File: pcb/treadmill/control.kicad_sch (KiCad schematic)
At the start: 42 parts, among them J6 TO-DISPLAY, J7 JK1 (PROG), J8 MOTOR, Q3 "2T1" SS9012 PNP, Q4 "J3" SS9013 NPN, U4 STM8S003F3P, U5 EL817, U6 EL817, U7 LM358_DFN, U8 LM358_DFN

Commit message: Sustained progress reversing the pcb
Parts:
- added C13: C, symbol Device:C
- added C?: C_Polarized, symbol Device:C_Polarized
- added D3: LED, symbol Device:LED
- added Q11: "2T1" SS9012 PNP, symbol Simulation_SPICE:PNP
- added R14: 2k, symbol Device:R
- added R49: OL, symbol Device:R
- added U5: HL05, symbol Regulator_Linear:AZ1117-5.0
- added U8: EL817, Package_DIP:DIP-4_W7.62mm, symbol Isolator:EL817
- R50: value inf -> OL
- renumbered U5 to U6, U6 to U7
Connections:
- net +5V: now also D3.2 (A)
- net GND: now also C13.2, U5.1 (GND), U8.2
- net at R12.2, U6.1: now also C13.1, U5.2 (VO)
- net at C10.1: now also U5.3 (VI), U8.3
- net at R50.2: now also U8.4
- new net: R49.1, U8.1
- new net: D3.1 (K), R14.2
- new net: C?.2, R49.2
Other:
- moved on the sheet: BR1, C10, C14, C15, C17, C18, C19, C20, C23, C27, C3, C31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

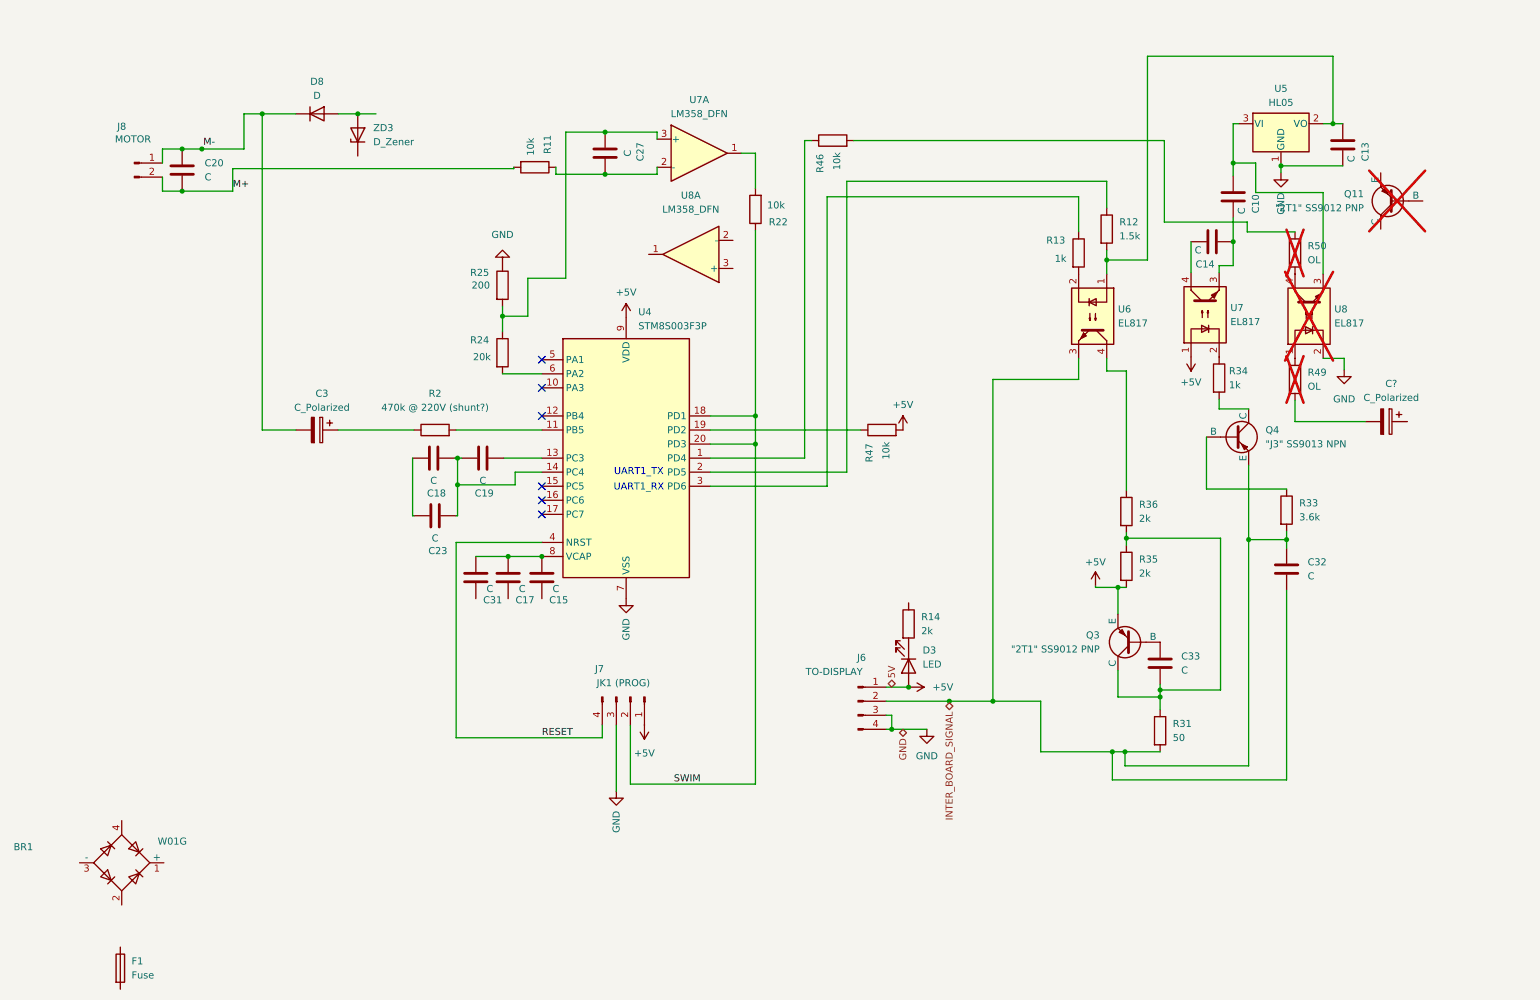
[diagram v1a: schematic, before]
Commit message: Figuring out more connections from the control board, mostly
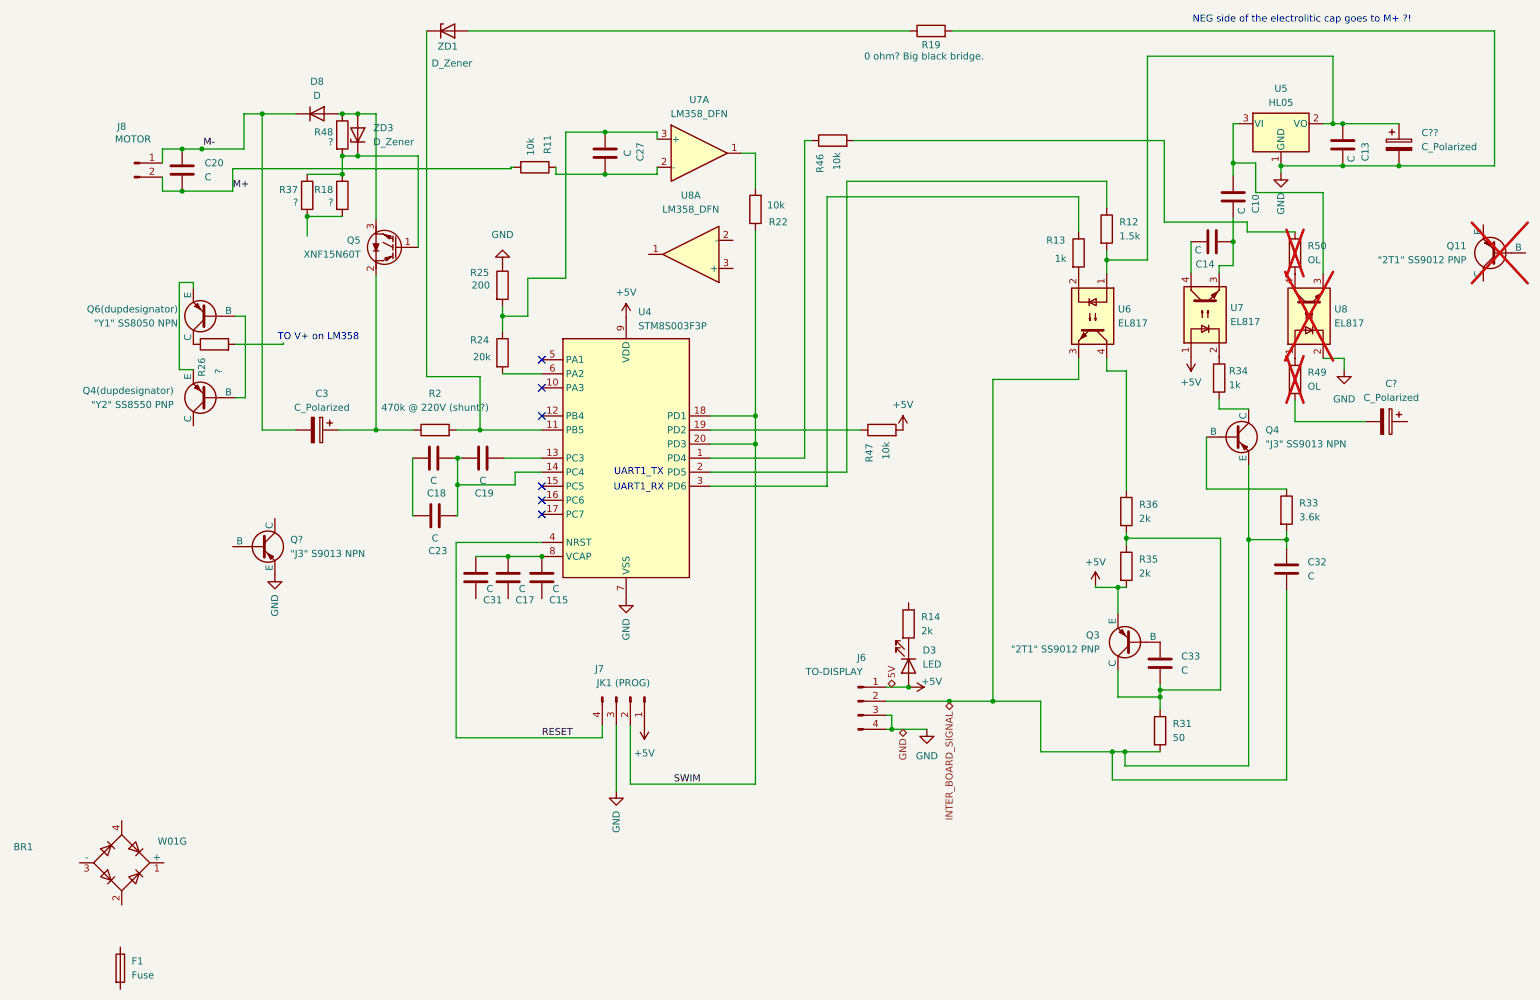
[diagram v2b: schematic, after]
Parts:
- added C??: C_Polarized, symbol Device:C_Polarized
- added Q4(dupdesignator): "Y2" SS8550 PNP, symbol Simulation_SPICE:PNP
- added Q5: XNF15N60T, Package_TO_SOT_THT:TO-220-3_Vertical, symbol Transistor_IGBT:STGP7NC60HD
- added Q6(dupdesignator): "Y1" SS8050 NPN, symbol Simulation_SPICE:PNP
- added Q?: "J3" S9013 NPN, symbol Simulation_SPICE:PNP
- added R18, R26, R37, R48: ?, symbol Device:R
- added R19: 0 ohm? Big black bridge., symbol Device:R
- added ZD1: D_Zener, symbol Device:D_Zener
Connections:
- net GND: now also C??.2, Q?.3 (E), R19.2
- net at ZD3.1 (K): now also Q5.1 (G), R18.1, R37.1, R48.2
- net at D8.2 (A), ZD3.2 (A): now also Q5.3 (E), R48.1
- net at C13.1, R12.2, U5.2 (VO)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: now also C??.1
- net at C3.1, R2.1: now also Q5.2 (C)
- net at R2.2, U4.11 (PB5): now also ZD1.1 (K)
- new net: Q6(dupdesignator).1 (C), R26.1
- new net: Q4(dupdesignator).2 (B), Q6(dupdesignator).2 (B)
- new net: Q4(dupdesignator).3 (E), Q6(dupdesignator).3 (E)
- new net: R19.1, ZD1.2 (A)
- new net: R18.2, R37.2
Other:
- note added: "NEG side of the electrolitic cap goes to M+ ?!"
- note added: "TO V+ on LM358"
- moved on the sheet: Q11
